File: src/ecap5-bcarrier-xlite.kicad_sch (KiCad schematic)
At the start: 43 parts, among them J3 Conn_01x04, J4 Conn_01x04, J5 USB_C_Receptacle_USB2.0_14P, J6 Conn_Coaxial, J7 Conn_Coaxial, J8 Conn_Coaxial, J9 1935161, Q1 BC846BR13, Q2 BC846BR13, SW1 RESET_SOM1, SW2 RESET_SOM2, SW3 USER1, SW4 USER1, U2 AP7375-33SA-7

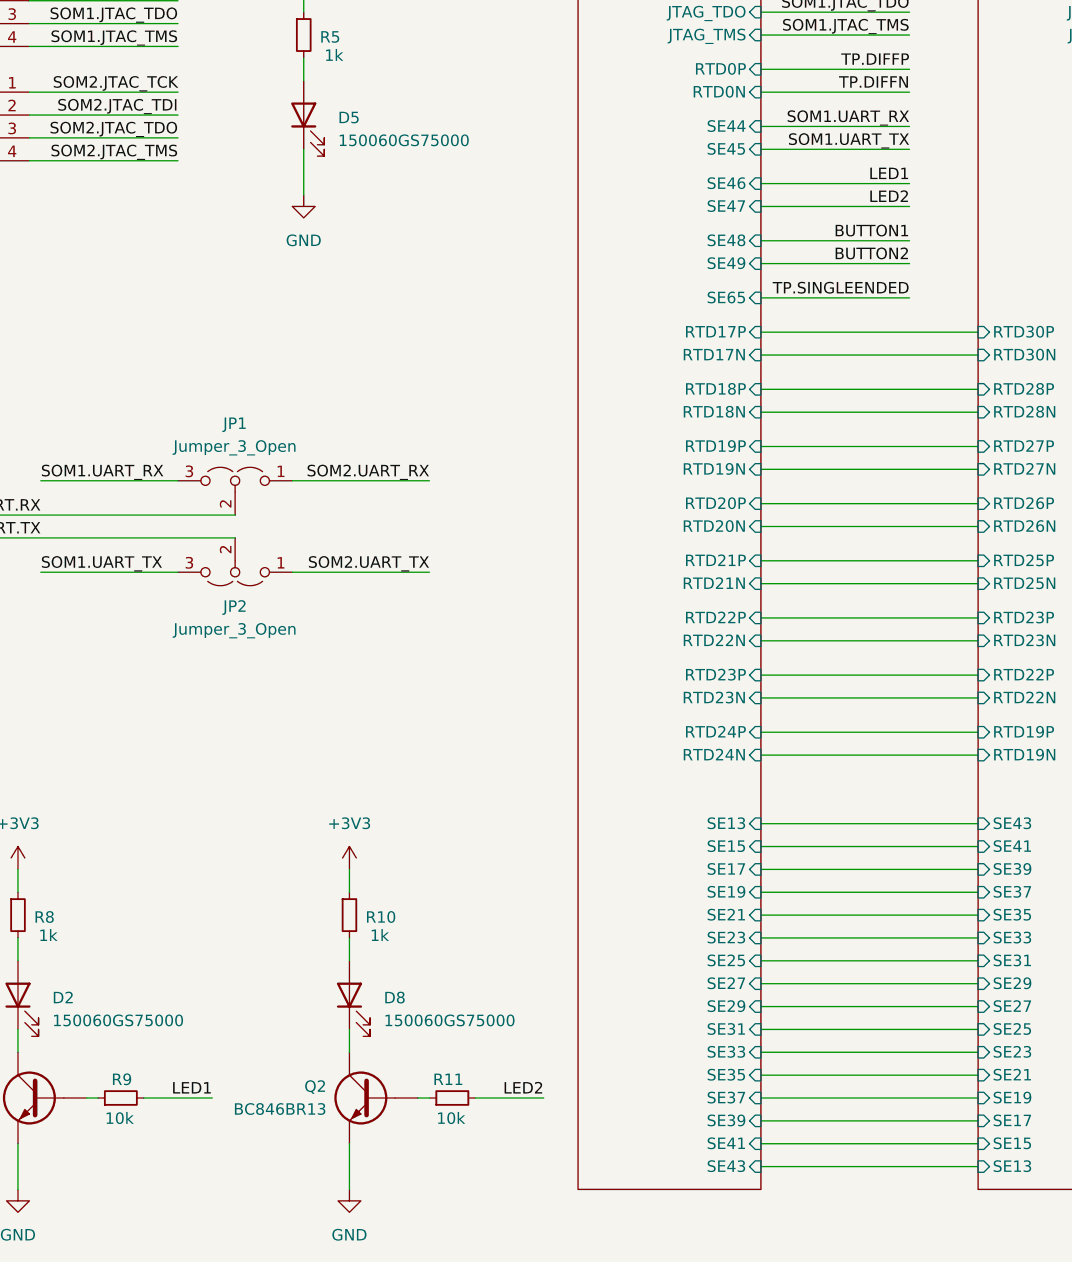
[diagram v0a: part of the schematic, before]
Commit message: Add silkscreen
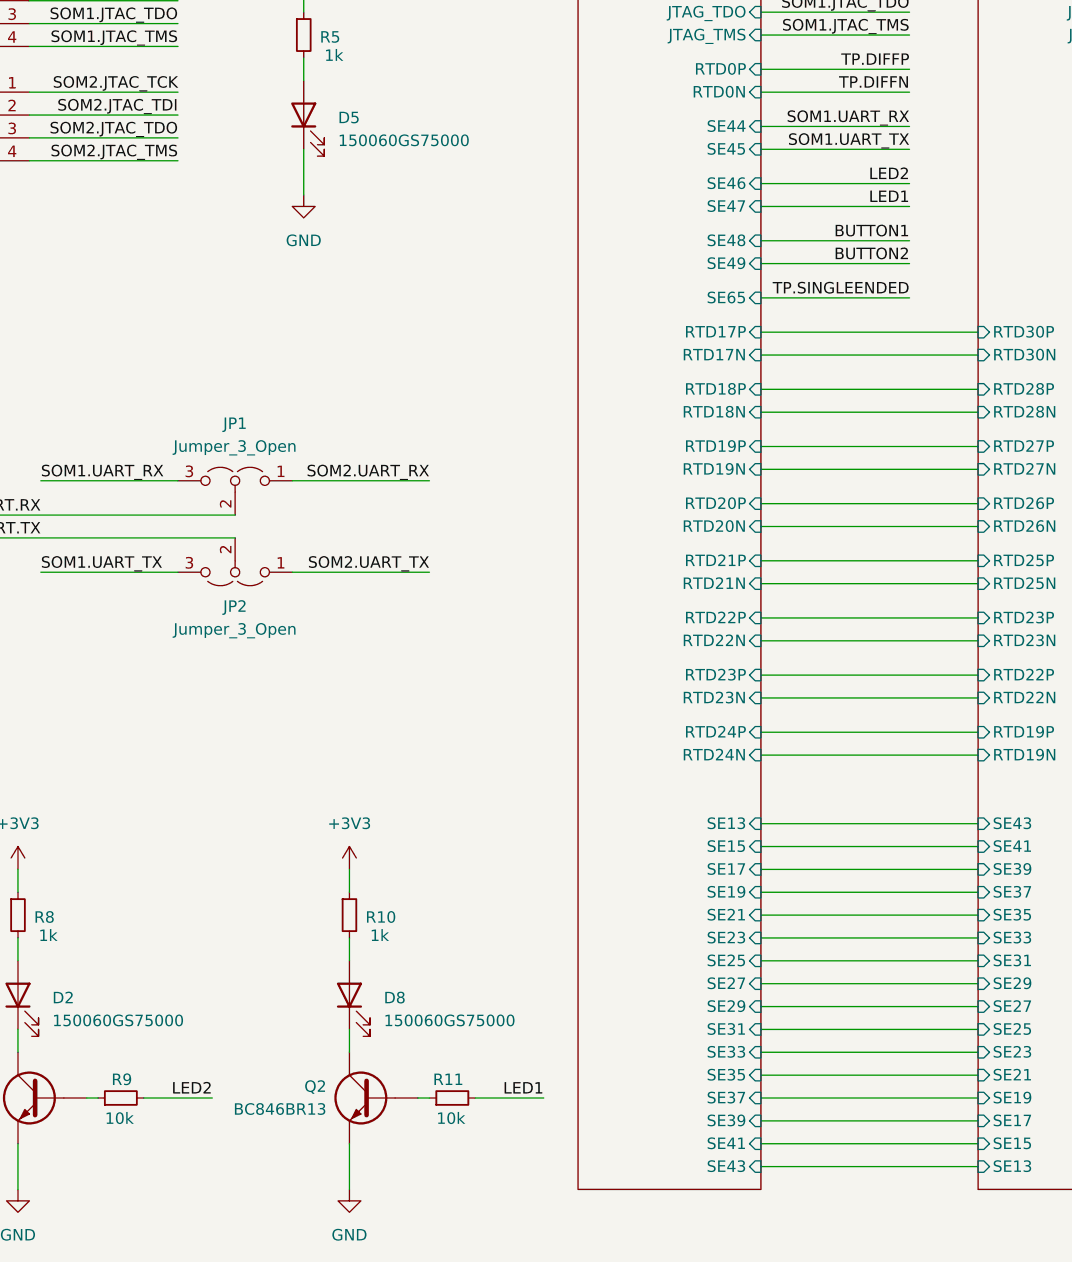
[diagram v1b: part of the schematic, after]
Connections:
- net LED1: now also R11.2; no longer R9.2
- net LED2: now also R9.2; no longer R11.2
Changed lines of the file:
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@@
 	)
 	(label "LED1"
-		(at 241.3 50.8 180)
+		(at 241.3 53.34 180)
 		(effects
 			(font
@@
 	)
 	(label "LED2"
-		(at 241.3 53.34 180)
+		(at 241.3 50.8 180)
 		(effects
 			(font
@@
 		)
 	)
-	(label "LED2"
+	(label "LED1"
 		(at 200.66 152.4 180)
 		(effects
@@
 		)
 	)
-	(label "LED1"
+	(label "LED2"
 		(at 163.83 152.4 180)
 		(effects

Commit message: Fix erc issues
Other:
- moved on the sheet: FB1

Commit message: Save button footprint in local library
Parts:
- SW1, SW2, SW3, SW4: footprint Button_Switch_SMD:SW_Push_1P1T_NO_CK_PTS125Sx73SMTR -> ECAP5-BCARRIER-XLITE:SW_Push_1P1T_NO_CK_PTS125Sx73SMTR_1
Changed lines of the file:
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@@
 			)
 		)
-		(property "Footprint" "Button_Switch_SMD:SW_Push_1P1T_NO_CK_PTS125Sx73SMTR"
+		(property "Footprint" "ECAP5-BCARRIER-XLITE:SW_Push_1P1T_NO_CK_PTS125Sx73SMTR_1"
 			(at 107.95 125.73 0)
 			(effects
@@
 			)
 		)
-		(property "Footprint" "Button_Switch_SMD:SW_Push_1P1T_NO_CK_PTS125Sx73SMTR"
+		(property "Footprint" "ECAP5-BCARRIER-XLITE:SW_Push_1P1T_NO_CK_PTS125Sx73SMTR_1"
 			(at 72.39 125.73 0)
 			(effects
@@
 			)
 		)
-		(property "Footprint" "Button_Switch_SMD:SW_Push_1P1T_NO_CK_PTS125Sx73SMTR"
+		(property "Footprint" "ECAP5-BCARRIER-XLITE:SW_Push_1P1T_NO_CK_PTS125Sx73SMTR_1"
 			(at 109.22 147.32 0)
 			(effects
@@
 			)
 		)
-		(property "Footprint" "Button_Switch_SMD:SW_Push_1P1T_NO_CK_PTS125Sx73SMTR"
+		(property "Footprint" "ECAP5-BCARRIER-XLITE:SW_Push_1P1T_NO_CK_PTS125Sx73SMTR_1"
 			(at 73.66 147.32 0)
 			(effects

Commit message: Improve the schematic
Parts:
- removed D6, D7: 150060GS75000, LED_SMD:LED_0603_1608Metric, symbol Device:LED
- removed R6, R7: 1k, Resistor_SMD:R_0603_1608Metric, symbol Device:R_Small
- C1: MPN (none) -> CL10A105KB8NNNC
- C2: MPN (none) -> CL10A106KP8NNNC
- D1: value VS-30MQ040-M3/5AT -> SS34; MPN (none) -> SS34
- D2, D5, D8: MPN (none) -> 150060GS75000
- D3, D4: MPN (none) -> ESD321DYAR
- D9: value P4SMAJ15CA -> SMAJ15CA/TR13; MPN (none) -> SMAJ15CA/TR13
- FB1: MPN (none) -> GZ2012D601TF
- J5: MPN (none) -> USB4105-GF-A-060
- J6, J7, J8: MPN (none) -> 132134-10
- J9: value 1935161 -> WJ127-5.0-2P; MPN (none) -> WJ127-5.0-2P
- JP1, JP2: now in the parts list
- Q1, Q2: value BC846BR13 -> MMBT4401; MPN (none) -> MMBT4401
- R1, R2: MPN (none) -> 0603WAF5101T5E
- R10, R5, R8: MPN (none) -> 0603WAF1001T5E
- R11, R12, R13, R9: MPN (none) -> 0603WAF1002T5E
- SW1, SW2, SW3, SW4: footprint ECAP5-BCARRIER-XLITE:SW_Push_1P1T_NO_CK_PTS125Sx73SMTR_1 -> Button_Switch_SMD:SW_Push_1P1T_NO_CK_PTS125Sx43PSMTR
- U2: MPN (none) -> AP7375-33SA-7
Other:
- sheet USB to UART ports: added none; removed ~{RXLED}, ~{TXLED}
- title: (none) -> ECAP5-BCARRIER-XLITE
- moved on the sheet: D2, D5, D8, H1, H2, H3, H4, J3, J4, J6, J7, J8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
